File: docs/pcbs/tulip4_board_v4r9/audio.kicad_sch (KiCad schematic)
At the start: 28 parts, among them J2 SJ2-35863B1, U4 PCM5101A-Q1, U5 TPA6110A2DGN

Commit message: Progress routing
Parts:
- renumbered C15 to C?, C7 to C?, C18 to C?, C14 to C?, C20 to C?, C12 to C?, C17 to C?, C8 to C?, C11 to C?, C13 to C?, C10 to C?, C16 to C?, C19 to C?, C22 to C?, C9 to C?, C23 to C?, C6 to C?, C21 to C?, J2 to J?, R6 to R?, R10 to R?, R7 to R?, R8 to R?, R5 to R?, R9 to R?, U4 to U?, U5 to U?, VR1 to VR?

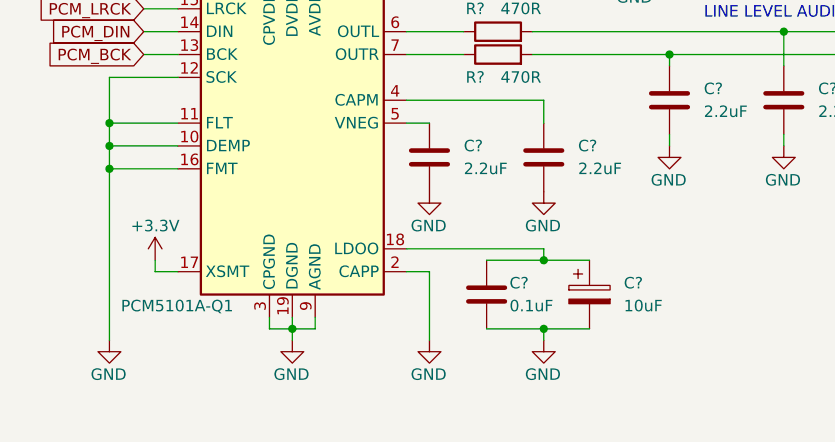
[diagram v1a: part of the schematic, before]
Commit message: V4R9A: USB, Audio circuit fix. Updated component part #s.
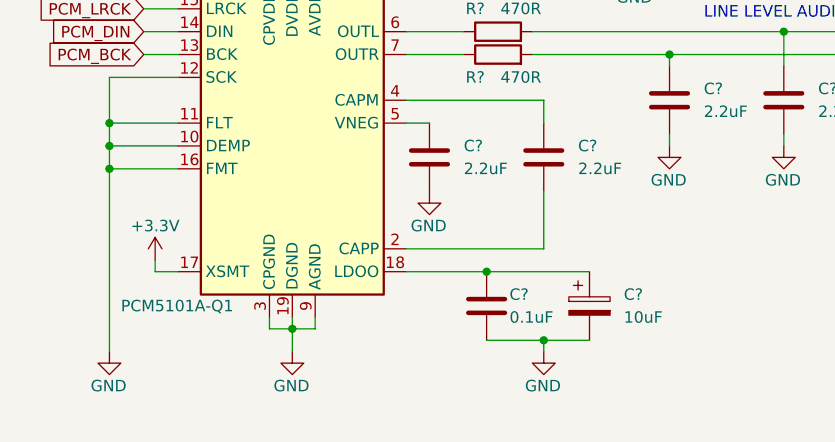
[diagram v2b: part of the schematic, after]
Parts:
- removed C?: 10uF, tulipcc_footprint_lib:CAP_WE_865060340001, symbol tulipcc_symbol_lib:CAP_10UF_16V
- removed C?: 0.1uF, tulipcc_footprint_lib:C_0805_2012, symbol tulipcc_symbol_lib:CAP_0805_0.1UF
- added C?: 10uF, tulipcc_footprint_lib:CAP_WE_865060340001, symbol tulipcc_symbol_lib:CAP_10UF_16V
- added C?: 0.1uF, tulipcc_footprint_lib:C_0805_2012, symbol tulipcc_symbol_lib:CAP_0805_0.1UF
- R? (x2): Part # CR0805-FX-4703ELF -> CR0805-FX-4700ELF; Supplier 1 # 652-CR0805FX-4703ELF -> 652-CR0805FX-4700ELF; Supplier 2 # 118-CMP1206-FX-4703ELFCT-ND -> CR0805-FX-4700ELFCT-ND
- U?: footprint Package_SO:TSSOP-20_4.4x6.5mm_P0.65mm -> tulipcc_footprint_lib:TSSOP-20_4.4x6.5mm_P0.65mm
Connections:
- net GND: now also C?.2, C?.2; no longer C?.2, U?.2 (CAPP)
- net at U?.18 (LDOO): now also C?.1, C?.1
- new net: C?.2, U?.2 (CAPP)
